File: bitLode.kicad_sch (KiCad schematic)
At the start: 30 parts, among them J1 USB_C_Receptacle_USB2.0, J2 Hashboard0, U2 W25Q16JVUXIQ, U3 RP2040, U4 AP2112K-3.3TRG1, Y1 12MHz

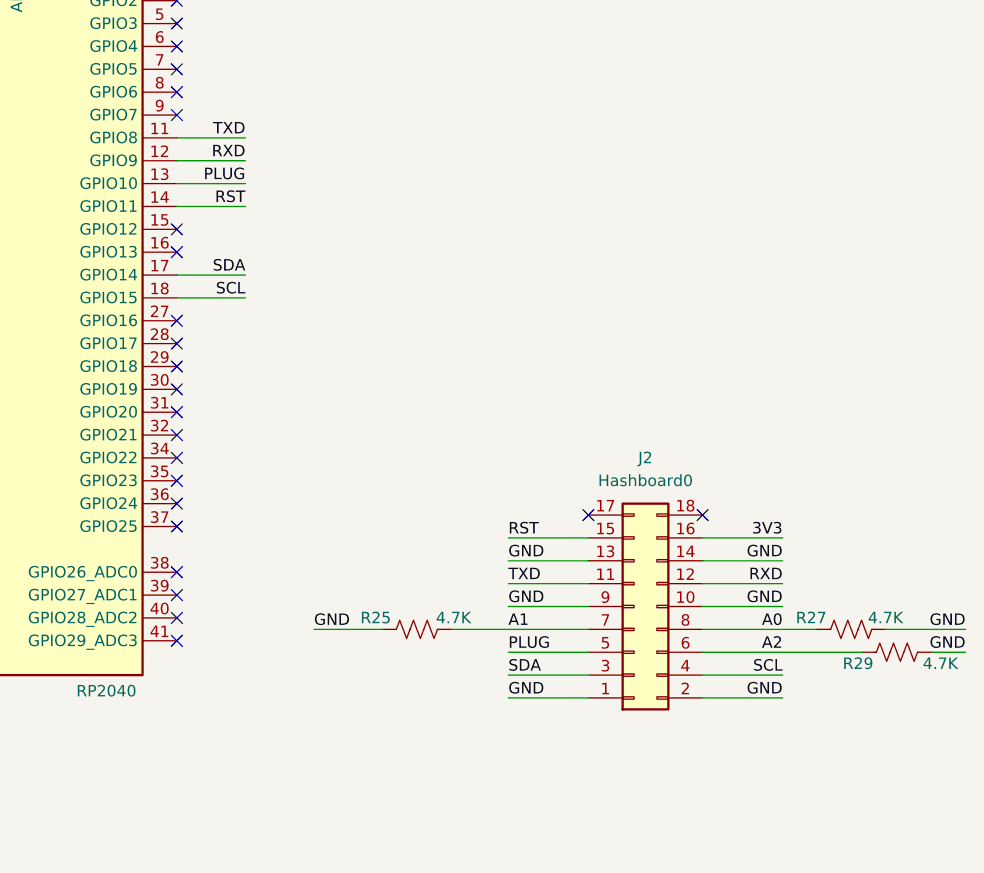
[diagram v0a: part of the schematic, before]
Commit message: First push of bitLoad interface board
Changes from Aditboard v2
- move to 7x2mm connector and changed connections appropriately
- changed logo on bottom silk to bitLode :)
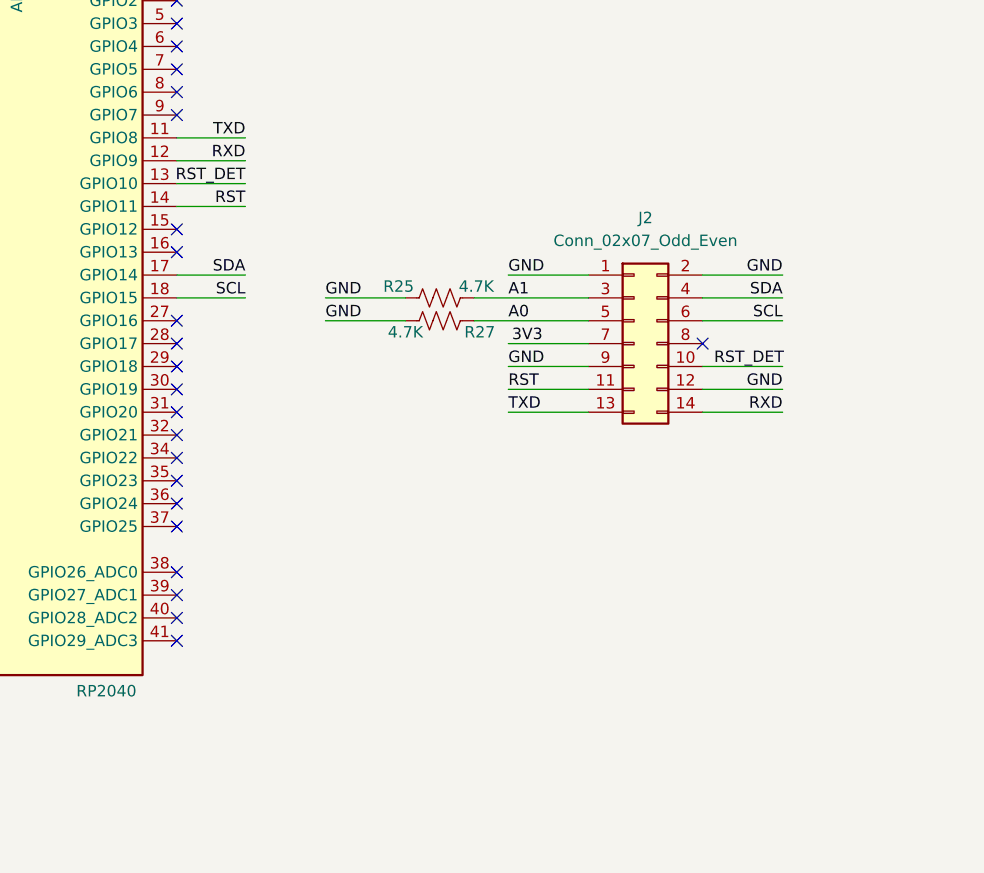
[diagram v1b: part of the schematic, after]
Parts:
- removed J2: Hashboard0, aditBoard:PinHeader_2x09_P2.00mm_Horizontal, symbol Connector_Generic:Conn_02x09_Odd_Even
- removed R29: 4.7K, Resistor_SMD:R_0402_1005Metric, symbol Device:R_US
- added J2: Conn_02x07_Odd_Even, Connector_PinSocket_2.00mm:PinSocket_2x07_P2.00mm_Horizontal, symbol Connector_Generic:Conn_02x07_Odd_Even
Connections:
- net 3V3: now also J2.7 (Pin_7)
- net A0: now also J2.5 (Pin_5)
- net A1: now also J2.3 (Pin_3)
- net GND: now also J2.1 (Pin_1), J2.12 (Pin_12), J2.2 (Pin_2), J2.9 (Pin_9)
- net RST: now also J2.11 (Pin_11)
- net RXD: now also J2.14 (Pin_14)
- net SCL: now also J2.6 (Pin_6)
- net SDA: now also J2.4 (Pin_4)
- net TXD: now also J2.13 (Pin_13)
- net PLUG renamed RST_DET
- net RST_DET: now also J2.10 (Pin_10)
- no-connect marks 26 -> 25
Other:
- moved on the sheet: R25, R27
